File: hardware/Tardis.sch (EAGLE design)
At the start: 49 parts, among them IC1 78LS05, IC2 ATMEGA328P-PU, IC3 ISD25120, J1 AUDIO IN, Q1 2N2222, Q2 N-CHAN, X1 LAMP, X2 POWER, X3 AMP PWR, X5 SPKR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

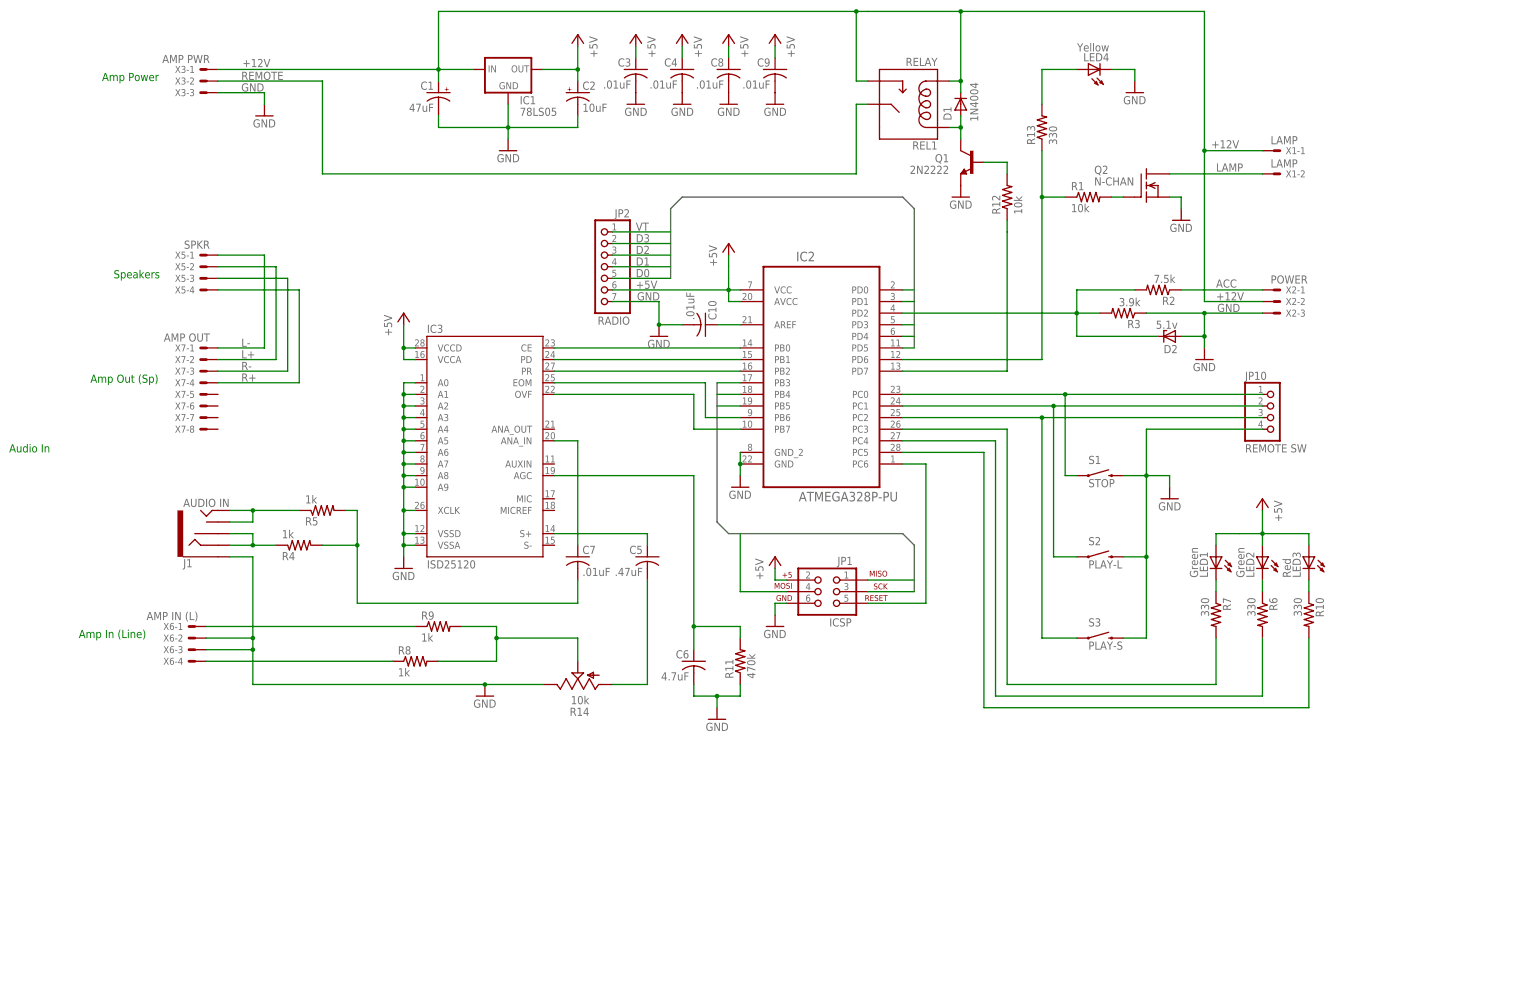
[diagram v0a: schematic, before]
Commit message: Add custom library.
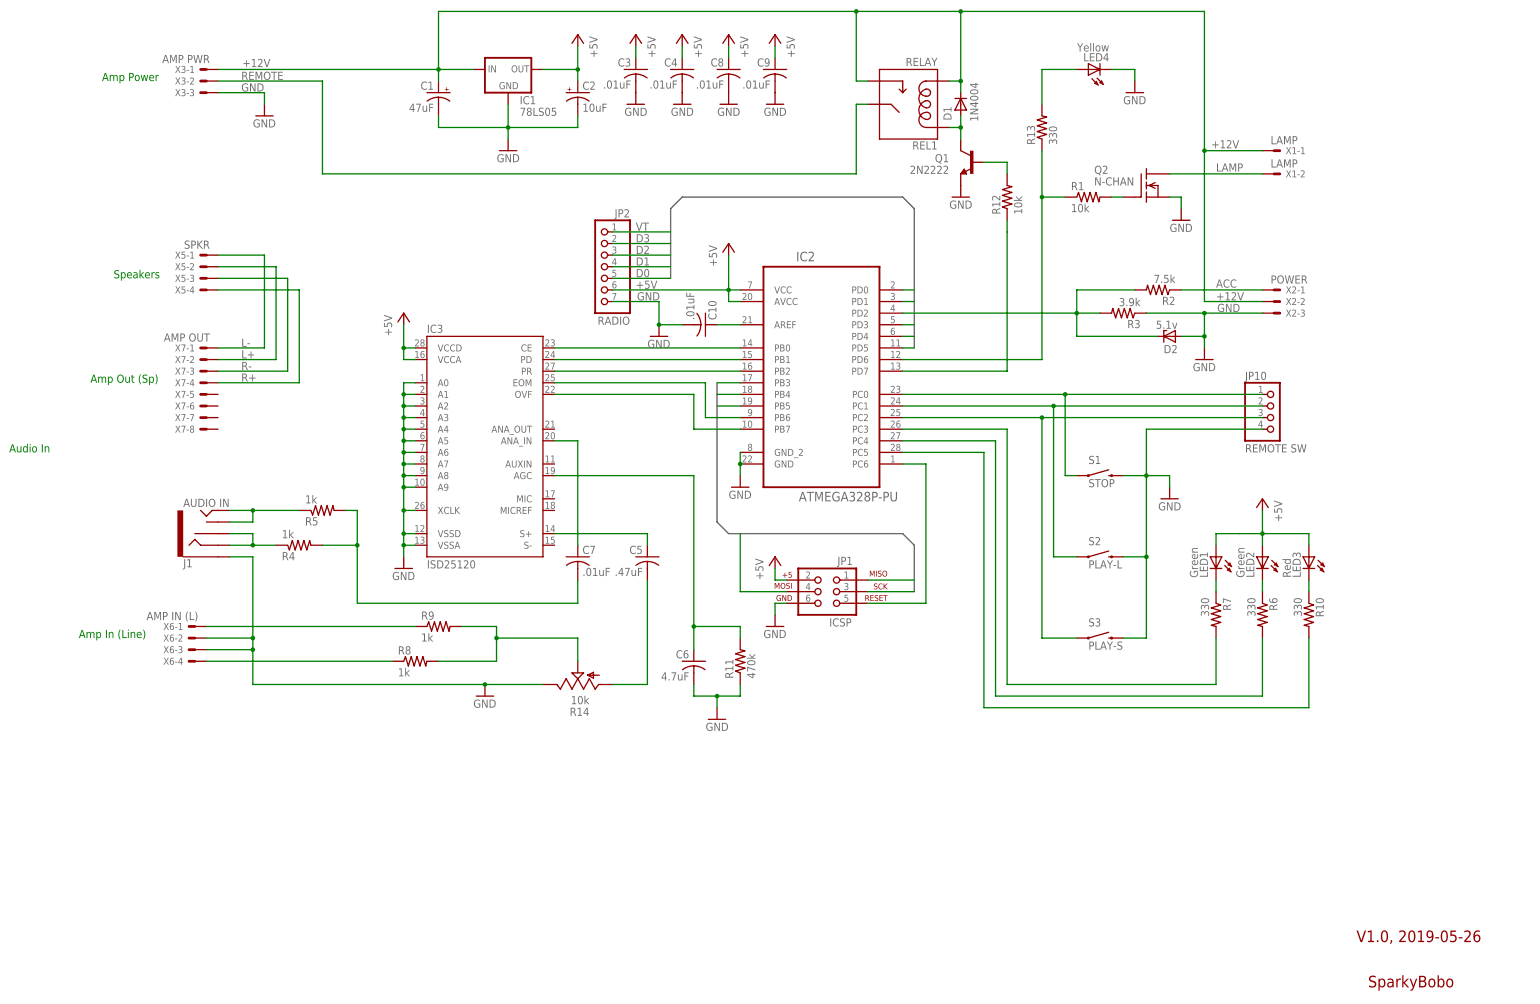
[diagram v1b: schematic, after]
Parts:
- IC2: device Atmel_By_element14_Batch_1:ATMEGA328P-PU -> CrazyGiraffe-Tardis:ATMEGA328P-PU
- IC3: device crazygiraffe:ISD25120 -> CrazyGiraffe-Tardis:CRAZYGIRAFFE_ISD25120
- REL1: device crazygiraffe:RELAY -> CrazyGiraffe-Tardis:CRAZYGIRAFFE_RELAY
- S1, S2, S3: device crazygiraffe:SWITCH-MOMENTARY-212MM -> CrazyGiraffe-Tardis:CRAZYGIRAFFE_SWITCH-MOMENTARY-212MM
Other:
- note added: "SparkyBobo"
- note added: "V1.0, 2019-05-26"
